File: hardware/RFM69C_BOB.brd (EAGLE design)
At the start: 30.5 x 20.3 mm, 12 parts, among them U1 RFM69

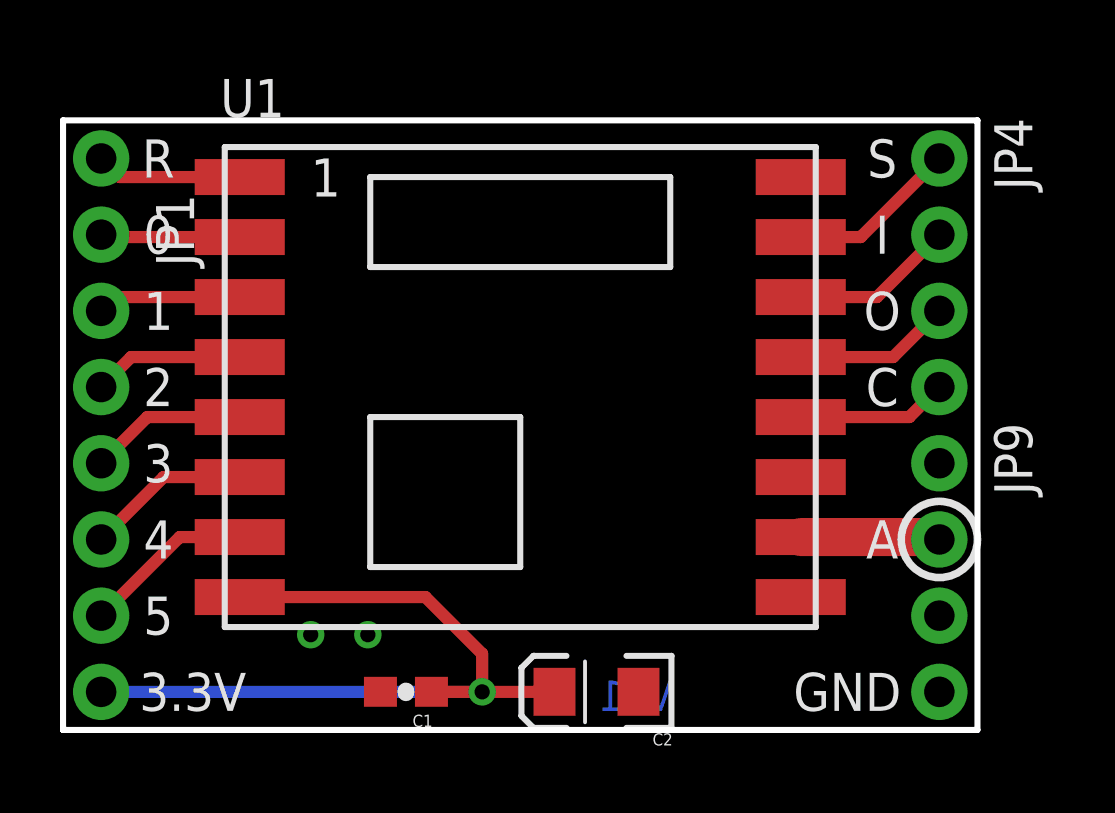
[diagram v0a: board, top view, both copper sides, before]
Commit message: Changed part to 'C' (compact) variant
New footprint, changed name to ensure proper variant is used (RFM69CW or
RFM69HCW)
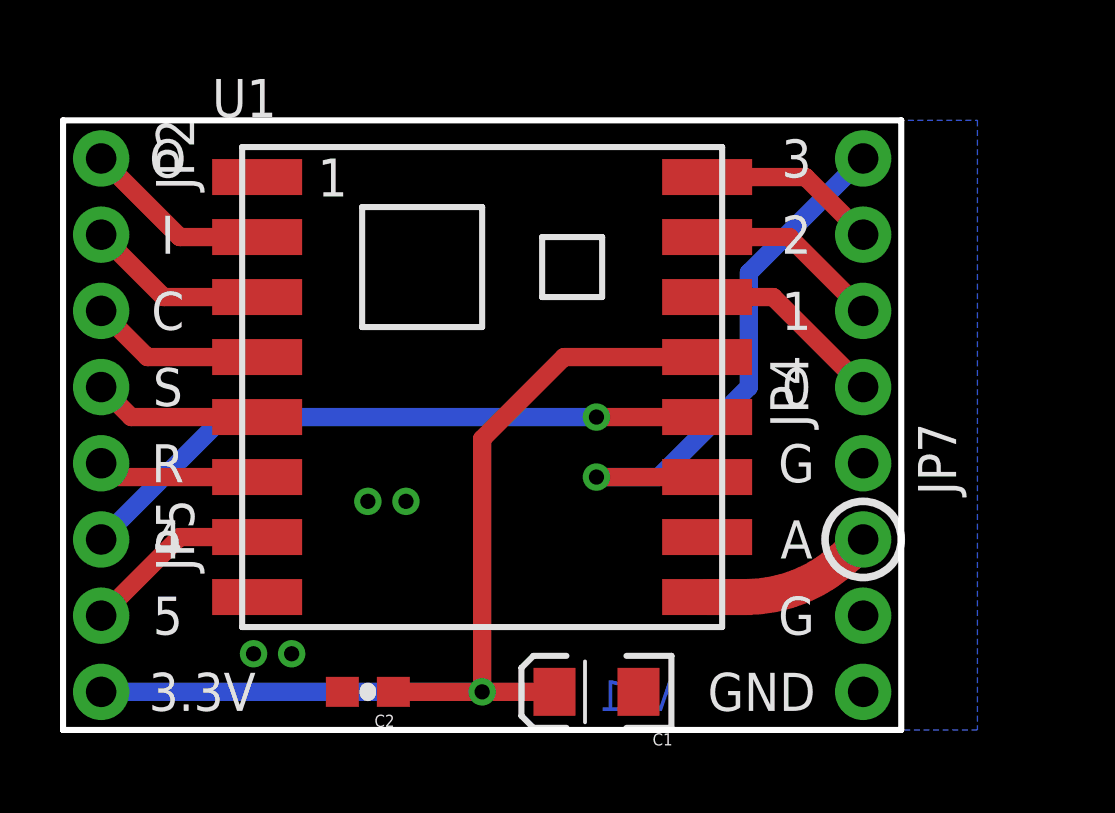
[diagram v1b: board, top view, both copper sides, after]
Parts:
- removed JP9: ANTENNA, mike-temp:1X03_ROUND_ONLY_NO_SILK
- added JP2: (no value), mike-temp:1X04_NO_SILK_ROUND
- added JP7: ANTENNA, mike-temp:1X03_ROUND_ONLY_NO_SILK
- C1: value 0.1uF -> 10uF; device SparkFun-Capacitors:0603-CAP -> SparkFun-Capacitors:EIA3216
- C2: value 10uF -> 0.1uF; device SparkFun-Capacitors:EIA3216 -> SparkFun-Capacitors:0603-CAP
- JP1: device mike-temp:1X06_NO_SILK_ROUND -> mike-temp:1X01NS
- JP5: device mike-temp:1X01NS -> mike-temp:1X02_NO_SILK
- U1: value RFM69 -> RFM69(H)CW; device mike-temp:RFM69 -> mike-temp:RFM69CS2
- moved JP1 15.2 mm to (1.27, 1.27), turned to 0 degrees
- moved JP3 10.2 mm to (1.27, 8.89)
- moved JP4 8.03 mm to (26.7, 11.4), turned to 90 degrees
- moved C2 7.62 mm to (10.2, 1.27)
- moved C1 6.35 mm to (17.8, 1.27)
- moved JP5 5.08 mm to (1.27, 6.35), turned to 270 degrees
- moved JP6 2.54 mm to (26.7, 1.27)
- moved LOGO1 1.27 mm to (20.3, 14.0)
- moved LOGO2 1.27 mm to (14.0, 11.4)
- moved U1 1.27 mm to (14.0, 11.4)
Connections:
- net 3.3V: now also C1.A, C2.1, JP1.1, U1.13; no longer C1.1, C2.A, JP5.1, U1.8
- net ANT: now also JP7.2, U1.9; no longer JP9.2, U1.10
- net DIO0: now also JP4.1, U1.14; no longer JP1.1, U1.2
- net DIO1: now also JP4.2, U1.15; no longer JP1.2, U1.3
- net DIO2: now also JP4.3, U1.16; no longer JP1.3, U1.4
- net DIO3: now also JP4.4, U1.11; no longer JP1.4, U1.5
- net DIO4: now also JP5.1, U1.12; no longer JP1.5, U1.6
- net DIO5: now also JP5.2; no longer JP1.6
- net GND: now also C1.C, C2.2, JP7.1, JP7.3, U1.1, U1.10, U1.8; no longer C1.2, C2.C, JP9.1, JP9.3, U1.11, U1.9
- net MISO: now also JP2.1, U1.2; no longer JP4.3, U1.13
- net MOSI: now also JP2.2, U1.3; no longer JP4.2, U1.14
- net NSS: now also JP2.4, U1.5; no longer JP4.1, U1.15
- net RESET: now also U1.6; no longer U1.1
- net SCK: now also JP2.3, U1.4; no longer JP4.4, U1.12
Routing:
- net DIO4: track 5.48 -> 21.9 mm, vias 0 -> 1
- net DIO3: track 5.26 -> 19.2 mm, vias 0 -> 1
- net 3.3V: track 26.9 -> 35.1 mm
- net DIO0: track 4.65 -> 6.44 mm
- net DIO1: track 4.81 -> 6.22 mm
- net ANT: track 4.65 -> 5.69 mm
- net MISO: track 5.26 -> 6.29 mm
- net DIO2: track 5.03 -> 6.00 mm
- net SCK: track 5.03 -> 5.84 mm
- net DIO5: track 5.71 -> 6.29 mm
- net MOSI: track 5.48 -> 6.06 mm
- net RESET: track 4.88 -> 5.39 mm
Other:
- board size 30.5 x 20.3 mm -> 27.9 x 20.3 mm
- board text added: "CW"
- board text added: "G"
- board text added: "HCW"
- board text added: "RFM69C"
- board text removed: "13dBm"
- board text removed: "20dBm"
- board text removed: "RFM69"
